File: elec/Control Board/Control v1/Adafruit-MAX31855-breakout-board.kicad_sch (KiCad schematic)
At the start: 3 parts

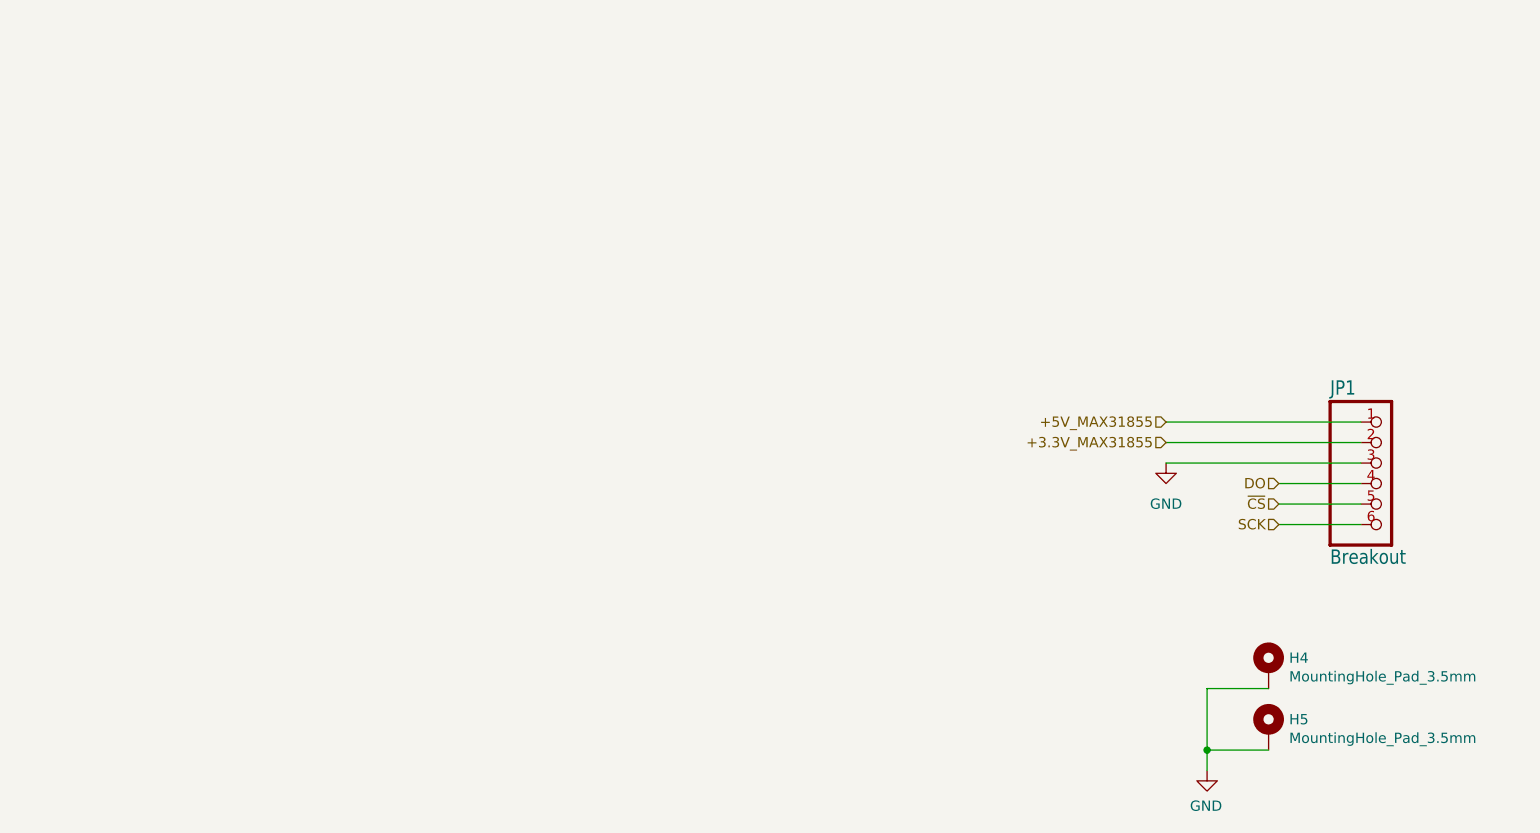
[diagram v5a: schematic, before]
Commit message: Add footprints for thermoucouple modules to schematic and PCB.  This commit does NOT capture the library changes.
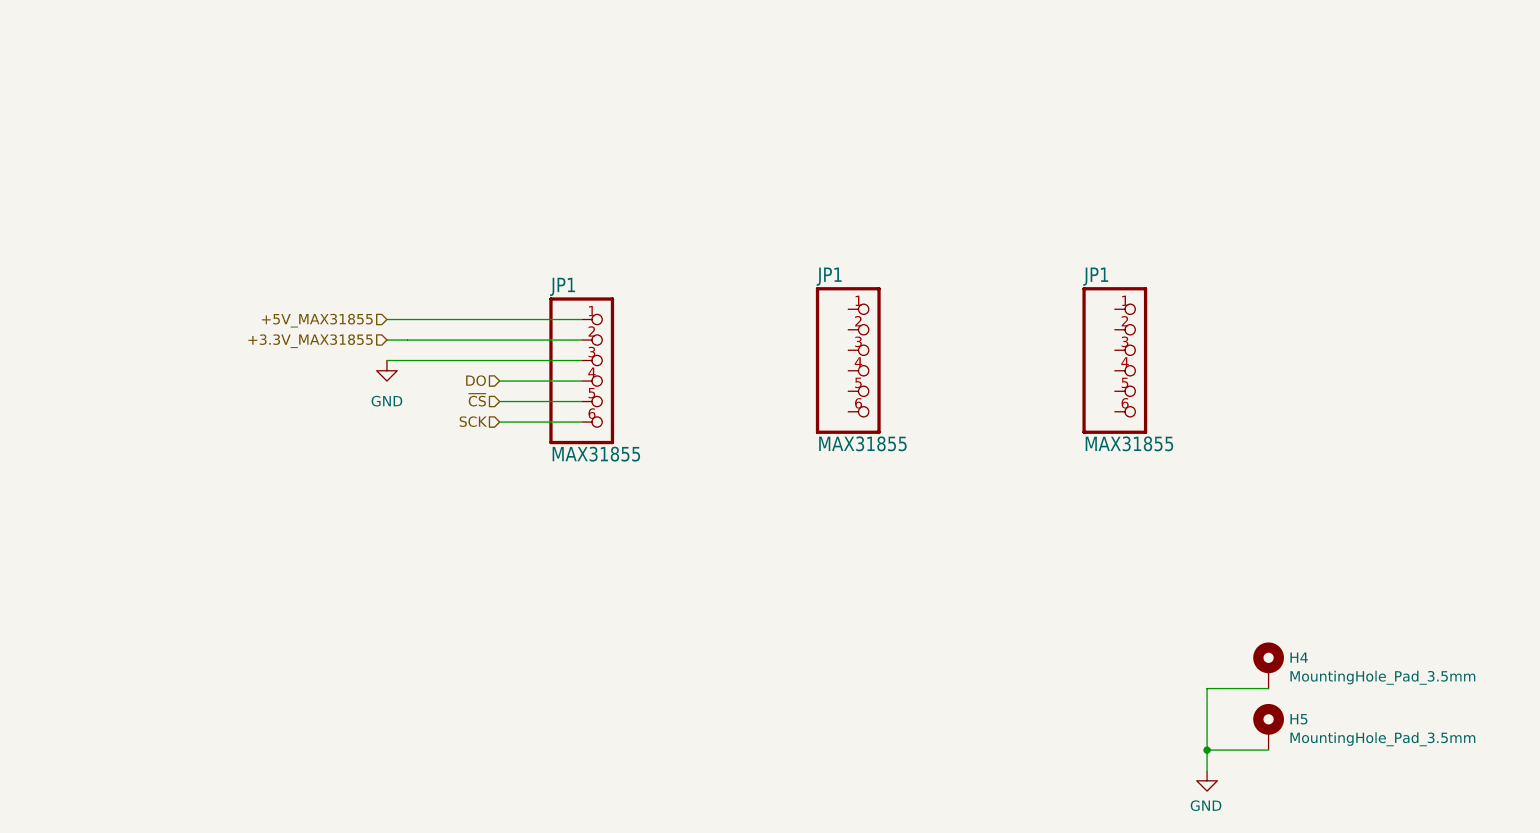
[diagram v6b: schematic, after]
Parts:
- added JP1 (x2): MAX31855, PubInv_KiCad_PCB:Adafruit_MAX31855_Module, symbol Control v1-eagle-import:HEADER-1X676MIL
- JP1: value Breakout -> MAX31855; footprint Control v1:1X06_ROUND_76 -> PubInv_KiCad_PCB:Adafruit_MAX31855_Module
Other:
- moved on the sheet: JP1
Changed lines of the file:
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@@
   (junction (at 179.07 157.48) (diameter 0) (color 0 0 0 0)
   )
-  (wire (pts (xy 176.53 119.38) (xy 198.12 119.38))
+  (wire (pts (xy 80.01 106.68) (xy 101.6 106.68))
     (stroke (width 0.1524) (type solid))
   )
-  (wire (pts (xy 173.99 116.84) (xy 198.12 116.84))
+  (wire (pts (xy 77.47 104.14) (xy 101.6 104.14))
     (stroke (width 0) (type default))
   )
-  (wire (pts (xy 173.99 121.92) (xy 198.12 121.92))
+  (wire (pts (xy 77.47 109.22) (xy 101.6 109.22))
     (stroke (width 0) (type default))
   )
-  (wire (pts (xy 187.96 124.46) (xy 198.12 124.46))
+  (wire (pts (xy 91.44 111.76) (xy 101.6 111.76))
     (stroke (width 0.1524) (type solid))
   )
@@
     (stroke (width 0) (type default))
   )
-  (wire (pts (xy 187.96 127) (xy 198.12 127))
+  (wire (pts (xy 91.44 114.3) (xy 101.6 114.3))
     (stroke (width 0.1524) (type solid))
   )
-  (wire (pts (xy 173.99 119.38) (xy 176.53 119.38))
+  (wire (pts (xy 77.47 106.68) (xy 80.01 106.68))
     (stroke (width 0) (type default))
   )
-  (wire (pts (xy 187.96 129.54) (xy 198.12 129.54))
+  (wire (pts (xy 91.44 116.84) (xy 101.6 116.84))
     (stroke (width 0.1524) (type solid))
   )
@@
     )
   )
-  (hierarchical_label "SCK" (shape input) (at 187.96 129.54 180) (fields_autoplaced)
+  (hierarchical_label "SCK" (shape input) (at 91.44 116.84 180) (fields_autoplaced)
     (effects (font (size 1.27 1.27)) (justify right))
   )
-  (hierarchical_label "DO" (shape input) (at 187.96 124.46 180) (fields_autoplaced)
+  (hierarchical_label "DO" (shape input) (at 91.44 111.76 180) (fields_autoplaced)
     (effects (font (size 1.27 1.27)) (justify right))
   )
-  (hierarchical_label "+3.3V_MAX31855" (shape input) (at 173.99 119.38 180) (fields_autoplaced)
+  (hierarchical_label "+3.3V_MAX31855" (shape input) (at 77.47 106.68 180) (fields_autoplaced)
     (effects (font (size 1.27 1.27)) (justify right))
   )
-  (hierarchical_label "+5V_MAX31855" (shape input) (at 173.99 116.84 180) (fields_autoplaced)
+  (hierarchical_label "+5V_MAX31855" (shape input) (at 77.47 104.14 180) (fields_autoplaced)
     (effects (font (size 1.27 1.27)) (justify right))
   )
-  (hierarchical_label "~{CS}" (shape input) (at 187.96 127 180) (fields_autoplaced)
+  (hierarchical_label "~{CS}" (shape input) (at 91.44 114.3 180) (fields_autoplaced)
     (effects (font (size 1.27 1.27)) (justify right))
   )
-  (symbol (lib_id "power:GND") (at 173.99 121.92 0) (unit 1)
+  (symbol (lib_id "power:GND") (at 77.47 109.22 0) (unit 1)
     (in_bom yes) (on_board yes) (dnp no) (fields_autoplaced)
-    (property "Reference" "#PWR024" (at 173.99 128.27 0)
+    (property "Reference" "#PWR024" (at 77.47 115.57 0)
       (effects (font (size 1.27 1.27)) hide)
     )
-    (property "Value" "GND" (at 173.99 127 0)
+    (property "Value" "GND" (at 77.47 114.3 0)
       (effects (font (size 1.27 1.27)))
     )
-    (property "Footprint" "" (at 173.99 121.92 0)
+    (property "Footprint" "" (at 77.47 109.22 0)
       (effects (font (size 1.27 1.27)) hide)
     )
-    (property "Datasheet" "" (at 173.99 121.92 0)
+    (property "Datasheet" "" (at 77.47 109.22 0)
       (effects (font (size 1.27 1.27)) hide)
     )
@@
     )
   )
+  (symbol (lib_id "Control v1-eagle-import:HEADER-1X676MIL") (at 170.18 110.49 0) (unit 1)
+    (in_bom yes) (on_board yes) (dnp no)
+    (property "Reference" "JP1" (at 163.83 99.695 0)
+      (effects (font (size 1.778 1.5113)) (justify left bottom))
+    )
+    (property "Value" "MAX31855" (at 163.83 120.65 0)
+      (effects (font (size 1.778 1.5113)) (justify left bottom))
+    )
+    (property "Footprint" "PubInv_KiCad_PCB:Adafruit_MAX31855_Module" (at 170.18 110.49 0)
+      (effects (font (size 1.27 1.27)) hide)
+    )
+    (property "Datasheet" "" (at 170.18 110.49 0)
+      (effects (font (size 1.27 1.27)) hide)
+    )
+    (pin "1")
+    (pin "2")
+    (pin "3")
+    (pin "4")
+    (pin "5")
+    (pin "6")
+    (instances
+      (project "Control v1"
+        (path "/acded065-8952-4dce-b7ce-b3a353c38348"
+          (reference "JP1") (unit 1)
+        )
+      )
+      (project "Control v1"
+        (path "/c68c9deb-8d4d-42f0-adf8-4d3022f4ee59/9d641288-e168-4964-816e-23e1814d1b66"
+          (reference "JP10") (unit 1)
+        )
+      )
+    )
+  )
   (symbol (lib_id "GPAD_SCH_LIB:MountingHole_Pad_3.5mm") (at 186.69 154.94 0) (unit 1)
     (in_bom yes) (on_board yes) (dnp no)
@@
     )
   )
+  (symbol (lib_id "Control v1-eagle-import:HEADER-1X676MIL") (at 137.16 110.49 0) (unit 1)
+    (in_bom yes) (on_board yes) (dnp no)
+    (property "Reference" "JP1" (at 130.81 99.695 0)
+      (effects (font (size 1.778 1.5113)) (justify left bottom))
+    )
+    (property "Value" "MAX31855" (at 130.81 120.65 0)
+      (effects (font (size 1.778 1.5113)) (justify left bottom))
+    )
+    (property "Footprint" "PubInv_KiCad_PCB:Adafruit_MAX31855_Module" (at 137.16 110.49 0)
+      (effects (font (size 1.27 1.27)) hide)
+    )
+    (property "Datasheet" "" (at 137.16 110.49 0)
+      (effects (font (size 1.27 1.27)) hide)
+    )
+    (pin "1")
+    (pin "2")
+    (pin "3")
+    (pin "4")
+    (pin "5")
+    (pin "6")
+    (instances
+      (project "Control v1"
+        (path "/acded065-8952-4dce-b7ce-b3a353c38348"
+          (reference "JP1") (unit 1)
+        )
+      )
+      (project "Control v1"
+        (path "/c68c9deb-8d4d-42f0-adf8-4d3022f4ee59/9d641288-e168-4964-816e-23e1814d1b66"
+          (reference "JP9") (unit 1)
+        )
+      )
+    )
+  )
   (symbol (lib_id "power:GND") (at 179.07 160.02 0) (mirror y) (unit 1)
     (in_bom yes) (on_board yes) (dnp no)
@@
     )
   )
-  (symbol (lib_id "Control v1-eagle-import:HEADER-1X676MIL") (at 200.66 124.46 0) (unit 1)
+  (symbol (lib_id "Control v1-eagle-import:HEADER-1X676MIL") (at 104.14 111.76 0) (unit 1)
     (in_bom yes) (on_board yes) (dnp no)
-    (property "Reference" "JP1" (at 194.31 113.665 0)
+    (property "Reference" "JP1" (at 97.79 100.965 0)
       (effects (font (size 1.778 1.5113)) (justify left bottom))
     )
-    (property "Value" "Breakout" (at 194.31 134.62 0)
+    (property "Value" "MAX31855" (at 97.79 121.92 0)
       (effects (font (size 1.778 1.5113)) (justify left bottom))
     )
-    (property "Footprint" "Control v1:1X06_ROUND_76" (at 200.66 124.46 0)
+    (property "Footprint" "PubInv_KiCad_PCB:Adafruit_MAX31855_Module" (at 104.14 111.76 0)
       (effects (font (size 1.27 1.27)) hide)
     )
-    (property "Datasheet" "" (at 200.66 124.46 0)
+    (property "Datasheet" "" (at 104.14 111.76 0)
       (effects (font (size 1.27 1.27)) hide)
     )
@@
       (project "Control v1"
         (path "/c68c9deb-8d4d-42f0-adf8-4d3022f4ee59/9d641288-e168-4964-816e-23e1814d1b66"
-          (reference "JP4") (unit 1)
+          (reference "JP8") (unit 1)
         )
       )

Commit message: Update schematic for MCP9600 I2C thermocouple.
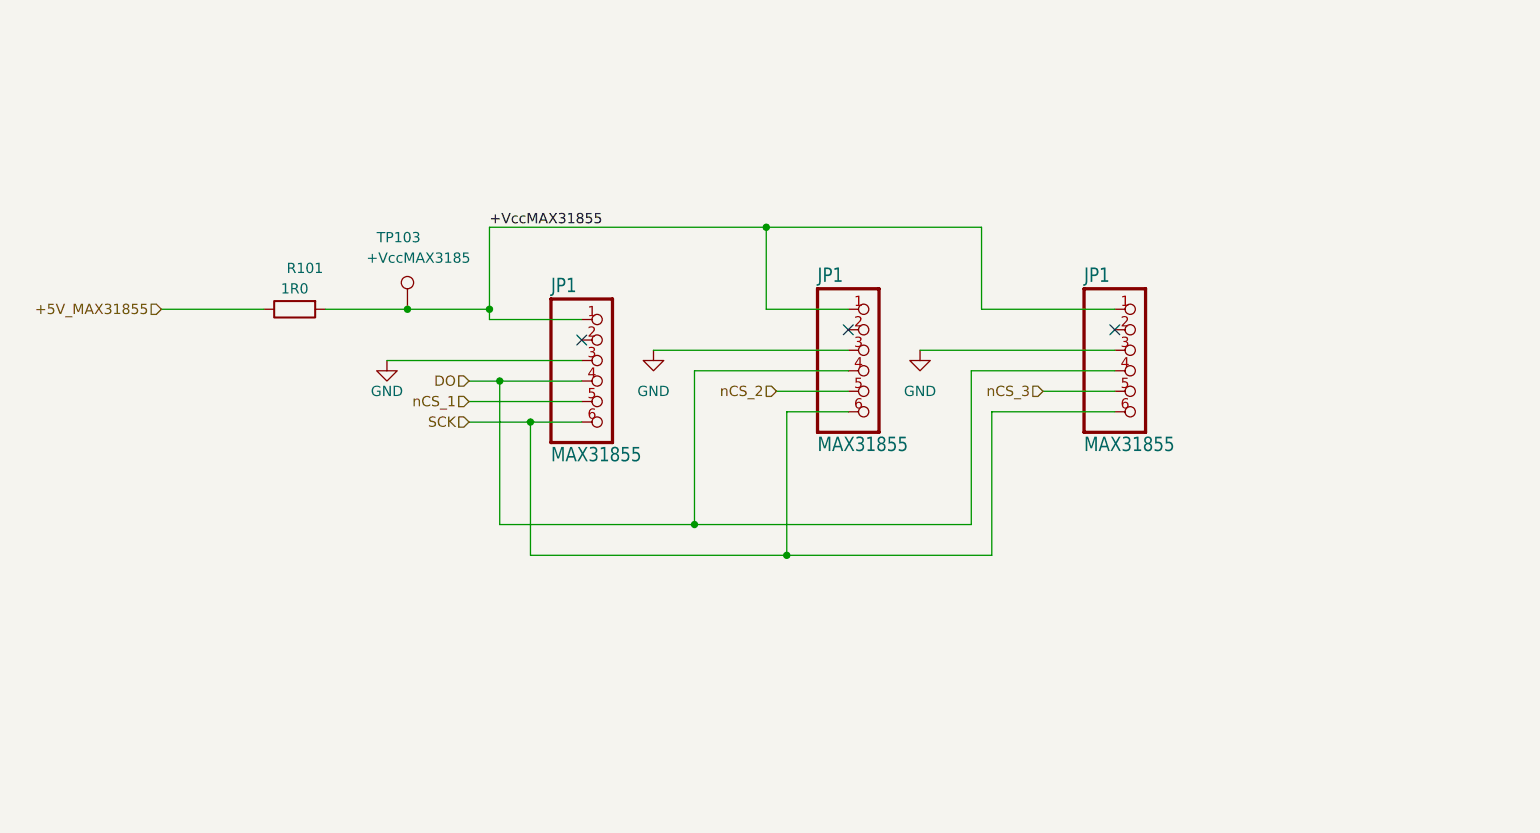
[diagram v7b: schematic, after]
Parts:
- removed H4, H5: MountingHole_Pad_3.5mm, GeneralPurposeAlarmDevicePCB:MountingHole_3.5mm_Pad_Via, symbol GPAD_SCH_LIB:MountingHole_Pad_3.5mm
- added R101: 1R0, Resistor_SMD:R_0603_1608Metric_Pad0.98x0.95mm_HandSolder, symbol Device:R
- added TP103: +VccMAX3185, TestPoint:TestPoint_Loop_D2.54mm_Drill1.5mm_Beaded, symbol Connector:TestPoint
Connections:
- net +5V_MAX31855: now also R101.1; no longer JP1.1
- net DO: now also JP1.4, JP1.4
- net GND: now also JP1.3, JP1.3
- net SCK: now also JP1.6, JP1.6
- net +VccMAX31855: now reaches JP1.1
- net +VccMAX31855: now also JP1.1, JP1.1, R101.2, TP103.1
- net nCS_3: now reaches JP1.5
- net nCS_2: now reaches JP1.5
- net +3.3V_MAX31855: no longer names the net of JP1.2
- net ~{CS} renamed nCS_1
- no-connect marks 0 -> 3
